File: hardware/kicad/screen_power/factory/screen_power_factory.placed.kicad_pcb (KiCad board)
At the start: 4 copper layers, 130 x 120 mm, 72 parts, among them J1 AUX 5V INPUT, J101 PI USB, J102 TOUCH, J103 SCREEN POWER 5V 3A, J2 SCREEN CONTROL, J201 PI USB, J202 TOUCH, J203 SCREEN POWER 5V 3A, Q1 MMBT3904,215, Q101 2N7002, Q102 2N7002, Q201 2N7002, Q202 2N7002, U101 ADuM3165BRSZ, U102 SN74LVC1G14DBVR, U103 TPS25221DBVR, U104 TPS25810RVCR, U201 ADuM3165BRSZ, U202 SN74LVC1G14DBVR, U203 TPS25221DBVR, U204 TPS25810RVCR, Y101 24MHz 10pF, Y201 24MHz 10pF

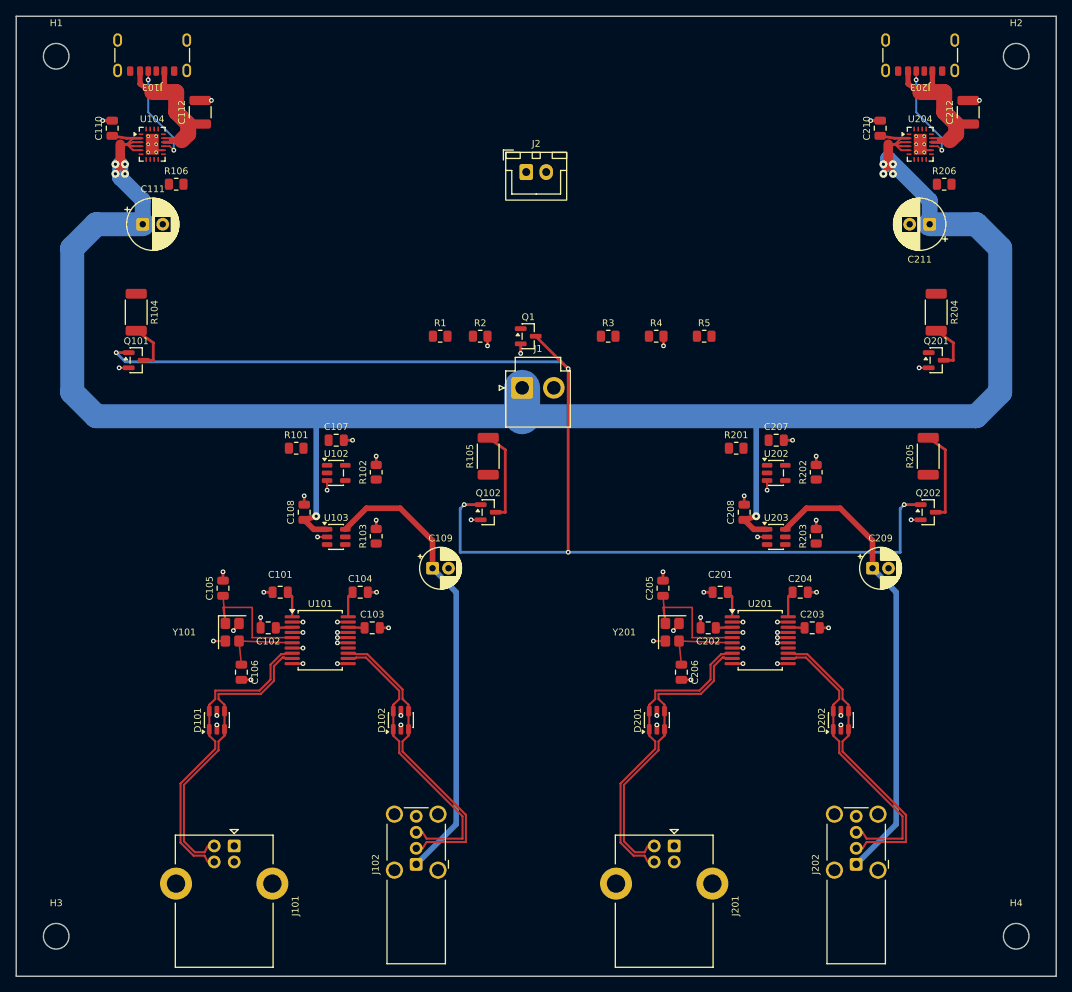
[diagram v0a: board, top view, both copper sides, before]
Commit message: refactor(hardware): simplify and compact screen power boards
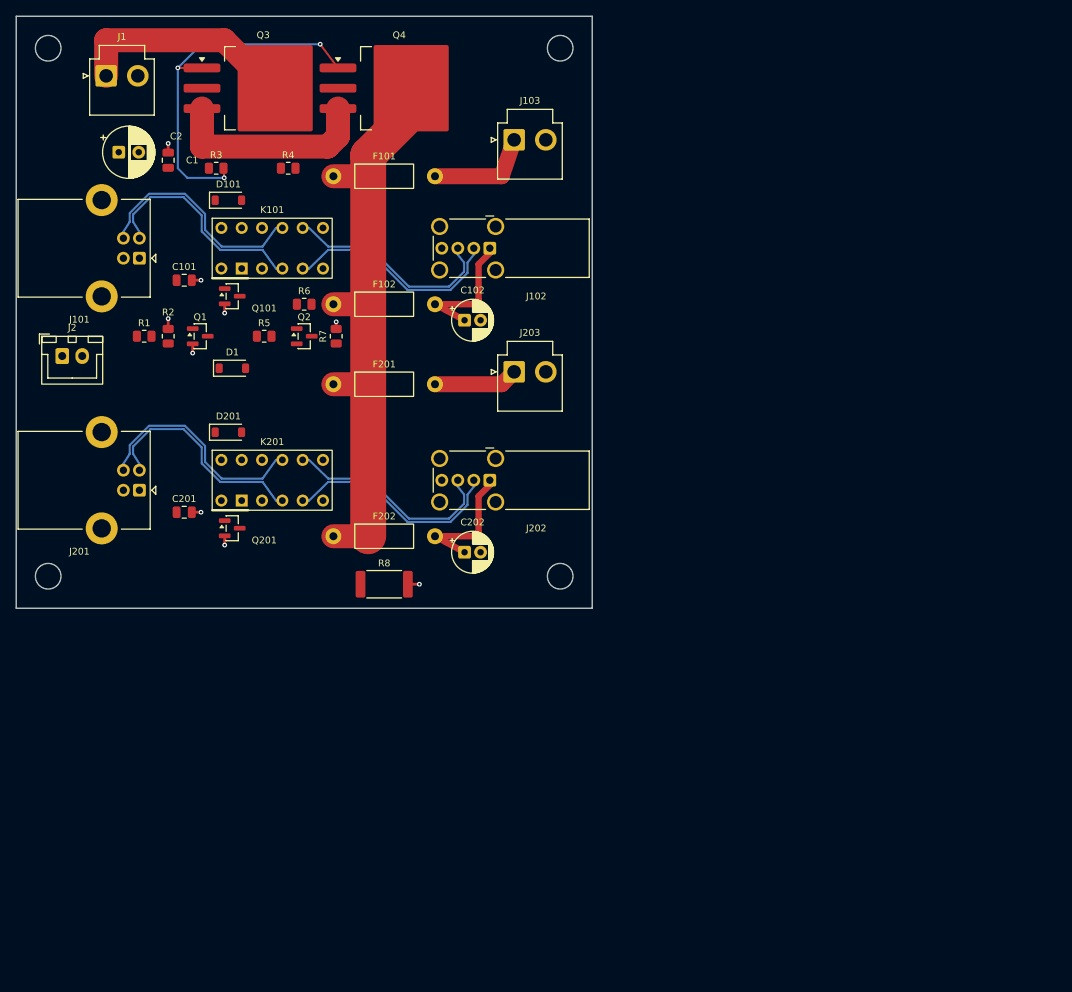
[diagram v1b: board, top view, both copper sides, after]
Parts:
- removed C103, C104, C107, C108, C110, C203, C204, C207, C208, C210: 100nF, C_0805_2012Metric
- removed C105, C106, C205, C206: 8pF C0G, C_0805_2012Metric
- removed C109, C209: 150uF 10V, CP_Radial_D5.0mm_P2.00mm
- removed C111, C211: 220uF 10V, CP_Radial_D6.3mm_P2.50mm
- removed C112, C212: 10uF 25V X7R, C_1210_3225Metric
- removed D102, D202: USBLC6-2SC6, SOT-23-6
- removed Q102, Q202: 2N7002, SOT-23
- removed R101, R102, R201, R202: 10k, R_0805_2012Metric
- removed R103, R203: 80.6k 1%, R_0805_2012Metric
- removed R104, R105, R204, R205: 100R 0.75W, R_2010_5025Metric
- removed R106, R206: 100k 1%, R_0805_2012Metric
- removed U101, U201: ADuM3165BRSZ, SSOP-20_5.3x7.2mm_P0.65mm
- removed U102, U202: SN74LVC1G14DBVR, SOT-23-5
- removed U103, U203: TPS25221DBVR, SOT-23-6
- removed U104, U204: TPS25810RVCR, Texas_RVC0020A_WQFN-20-1EP_3x4mm_P0.5mm_EP1.6x2.6mm_ThermalVias
- removed Y101, Y201: 24MHz 10pF, Crystal_SMD_3225-4Pin_3.2x2.5mm
- added C1: 100nF 50V, C_0805_2012Metric, F.Cu at (19.0, 18.0)
- added C2: 220uF 10V, CP_Radial_D6.3mm_P2.50mm, F.Cu at (12.8, 17.0)
- added D1: 1N4148W, D_SOD-123, F.Cu at (27.0, 44.0)
- added F101: 4A fast, Fuse_Littelfuse_251_P12.70mm, F.Cu at (39.6, 20.0)
- added F102: 750mA fast, Fuse_Littelfuse_251_P12.70mm, F.Cu at (39.6, 36.0)
- added F201: 4A fast, Fuse_Littelfuse_251_P12.70mm, F.Cu at (39.6, 46.0)
- added F202: 750mA fast, Fuse_Littelfuse_251_P12.70mm, F.Cu at (39.6, 65.0)
- added K101: G6K-2P-RF DC5, Relay_DPDT_Omron_G6K-2P-RF, F.Cu at (32.0, 29.0)
- added K201: G6K-2P-RF DC5, Relay_DPDT_Omron_G6K-2P-RF, F.Cu at (32.0, 58.0)
- added Q2: MMBT3906, SOT-23, F.Cu at (36.0, 40.0)
- added Q3: SUM70101EL, TO-263-3_TabPin2, F.Cu at (30.9, 9.00)
- added Q4: SUM70101EL, TO-263-3_TabPin2, F.Cu at (47.9, 9.00)
- added R6: 100k 1%, R_0805_2012Metric, F.Cu at (36.0, 36.0)
- added R7: 100k 1%, R_0805_2012Metric, F.Cu at (40.0, 40.0)
- added R8: 100R 1W 1%, R_2512_6332Metric, F.Cu at (46.0, 71.0)
- C101, C201: value 100nF -> 100nF 50V
- C102, C202: value 100nF -> 150uF 10V; footprint C_0805_2012Metric -> CP_Radial_D5.0mm_P2.00mm
- D101, D201: value USBLC6-2SC6 -> 1N4148W; footprint SOT-23-6 -> D_SOD-123
- J103: value SCREEN POWER 5V 3A -> SCREEN 1 POWER; footprint USB_C_Receptacle_GCT_USB4125-xx-x_6P_TopMnt_Horizontal -> JST_VH_B2P-VH_1x02_P3.96mm_Vertical
- J2: value SCREEN CONTROL -> GPIO17 / GND
- J203: value SCREEN POWER 5V 3A -> SCREEN 2 POWER; footprint USB_C_Receptacle_GCT_USB4125-xx-x_6P_TopMnt_Horizontal -> JST_VH_B2P-VH_1x02_P3.96mm_Vertical
- Q1: value MMBT3904,215 -> MMBT3904
- R1: value 1k -> 1k 1%
- R2: value 10k -> 100k 1%
- R3: value 10k -> 4.7k 1%
- R4: value 100k -> 330k 1%
- R5: value 10k -> 5.6k 1%
- moved Q201 90.5 mm to (27.0, 64.0)
- moved J201 80.3 mm to (15.4, 59.2), turned to 180 degrees
- moved J102 77.6 mm to (59.2, 29.0), turned to 180 degrees
- moved J101 74.4 mm to (15.4, 30.2), turned to 180 degrees
- moved H4 72.6 mm to (68.0, 70.0)
- moved C201 67.7 mm to (21.0, 62.0), turned to 0 degrees
- moved J202 66.4 mm to (59.2, 58.0), turned to 180 degrees
- moved J203 65.0 mm to (62.2, 44.5), turned to 0 degrees
- moved D101 65.0 mm to (26.5, 23.0), turned to 0 degrees
- moved J1 65.0 mm to (11.2, 7.45)
- moved D201 64.5 mm to (26.5, 52.0), turned to 0 degrees
- moved J2 62.4 mm to (5.75, 42.5)
- moved H2 57.0 mm to (68.0, 4.00)
- moved R5 55.0 mm to (31.0, 40.0)
- moved R3 53.3 mm to (25.0, 19.0)
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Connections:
- C102 pad 1: S1_VDD1 -> S1_TOUCH_5V
- C202 pad 1: S2_VDD1 -> S2_TOUCH_5V
- D101 pad 1: S1_UP_P -> HOST1_5V
- D101 pad 2: GND -> S1_DATA_COIL_LOW
- D201 pad 1: S2_UP_P -> HOST2_5V
- D201 pad 2: GND -> S2_DATA_COIL_LOW
- Q1 pad 1: DUMP_BASE -> CONTROL_BASE
- Q1 pad 3: DISCHARGE -> CONTROL_SINK
- Q101 pad 1: DISCHARGE -> DATA_ENABLE
- Q101 pad 3: S1_DUMP0 -> S1_DATA_COIL_LOW
- Q201 pad 1: DISCHARGE -> DATA_ENABLE
- Q201 pad 3: S2_DUMP0 -> S2_DATA_COIL_LOW
- R1 pad 2: DISPLAY_ENABLE -> CONTROL_BASE
- R2 pad 1: DISPLAY_ENABLE -> CONTROL_BASE
- R3 pad 1: DISPLAY_ENABLE -> CONTROL_SINK
- R3 pad 2: DUMP_BASE -> POWER_GATE
- R4 pad 1: DUMP_BASE -> POWER_GATE
- R4 pad 2: GND -> COMMON_SOURCE
- R5 pad 1: AUX_5V -> BUFFER_SINK
- R5 pad 2: DISCHARGE -> BUFFER_BASE
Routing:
- net AUX_5V: track 274.9 -> 28.0 mm, vias 10 -> 0
- net DISCHARGE: track 159.0 -> 0.00 mm, vias 5 -> 0
- net SWITCHED_5V: track 0.00 -> 75.6 mm
- net GND: track 74.2 -> 10.5 mm, vias 61 -> 9
- net POWER_GATE: track 0.00 -> 45.8 mm, vias 0 -> 3
- net S2_TOUCH_5V: track 61.3 -> 16.9 mm, vias 1 -> 0
- net S1_TOUCH_5V: track 61.3 -> 16.9 mm, vias 1 -> 0
- net COMMON_SOURCE: track 0.00 -> 25.8 mm
- net S2_XI: track 17.9 -> 0.00 mm
- net S1_XI: track 17.9 -> 0.00 mm
- net S2_MAIN_5V: track 27.8 -> 10.5 mm
- net S1_MAIN_5V: track 27.8 -> 13.1 mm
- net S1_CC2: track 12.7 -> 0.00 mm, vias 2 -> 0
- net S2_CC2: track 12.7 -> 0.00 mm, vias 2 -> 0
- net S2_DUMP1: track 11.6 -> 0.00 mm
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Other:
- board size 130 x 120 mm -> 72 x 74 mm
